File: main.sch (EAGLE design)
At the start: 18 parts, among them IC1 TINY45/85, U1 TMP102

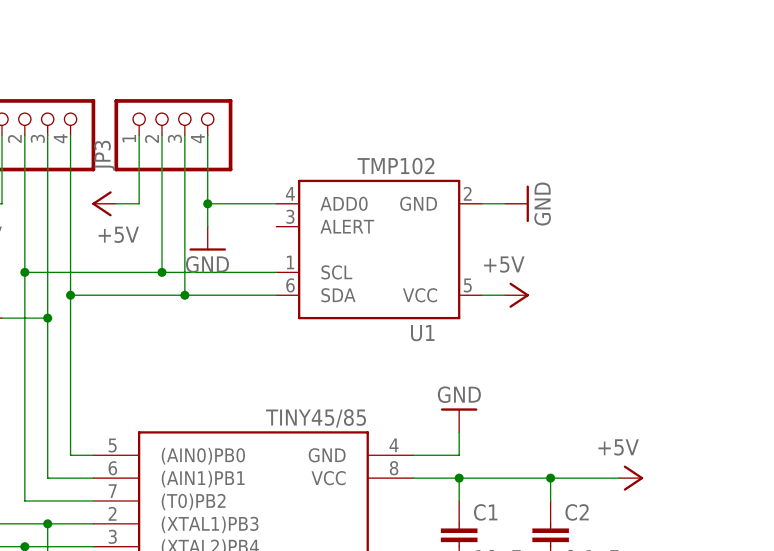
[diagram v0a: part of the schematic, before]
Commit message: changed sensor. sorted silk.
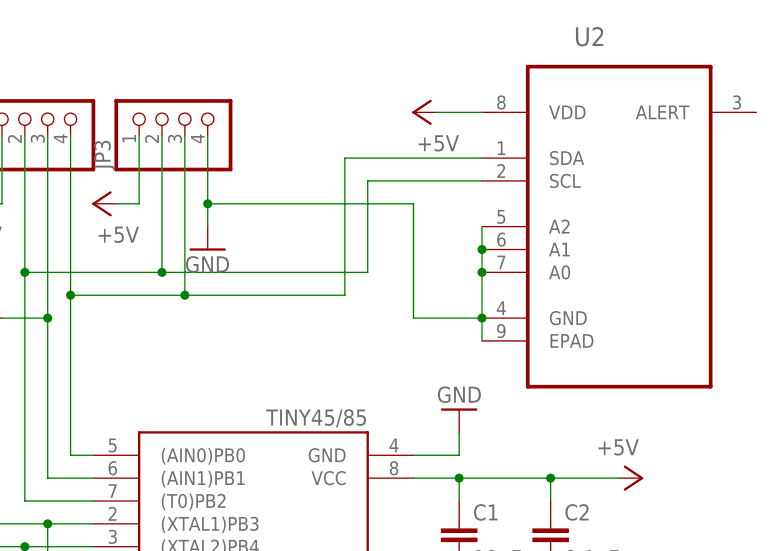
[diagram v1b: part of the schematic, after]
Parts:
- removed U1: TMP102, SparkFun-Sensors:TMP102
- added U2: MCP9808T-E/MC, mattsLib:MCP9808T-E/MC
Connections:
- net +5V: no longer U1.VCC
- net GND: now also U2.A0, U2.A1, U2.A2, U2.EPAD, U2.GND; no longer U1.ADD0, U1.GND
- net N$5: now also U2.SCL; no longer U1.SCL
- net N$9: now also U2.SDA; no longer U1.SDA
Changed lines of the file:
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@@
 <?xml version="1.0" encoding="utf-8"?>
 <!DOCTYPE eagle SYSTEM "eagle.dtd">
-<eagle version="7.2.0">
+<eagle version="7.0.0">
 <drawing>
 <settings>
@@
 <layer number="56" name="wert" color="7" fill="1" visible="no" active="no"/>
 <layer number="57" name="tCAD" color="7" fill="1" visible="no" active="no"/>
+<layer number="90" name="Modules" color="5" fill="1" visible="yes" active="yes"/>
 <layer number="91" name="Nets" color="2" fill="1" visible="yes" active="yes"/>
 <layer number="92" name="Busses" color="1" fill="1" visible="yes" active="yes"/>
@@
 <part name="GND8" library="supply1" deviceset="GND" device=""/>
 <part name="P+8" library="supply1" deviceset="+5V" device=""/>
-<part name="U1" library="SparkFun-Sensors" deviceset="TMP102" device="" value="TMP102"/>
-<part name="GND9" library="supply1" deviceset="GND" device=""/>
 <part name="CN1" library="adafruit" deviceset="USB" device="MINIB"/>
+<part name="U2" library="mattsLib" deviceset="MCP9808T-E/MC" device="" value=""/>
 </parts>
 <sheets>
@@
 <instance part="GND4" gate="1" x="-25.4" y="76.2" rot="R180"/>
 <instance part="GND5" gate="1" x="17.78" y="48.26" rot="R180"/>
-<instance part="P+5" gate="1" x="76.2" y="91.44" rot="R270"/>
+<instance part="P+5" gate="1" x="63.5" y="111.76" rot="R90"/>
 <instance part="P+6" gate="1" x="12.7" y="101.6" rot="R90"/>
 <instance part="GND6" gate="1" x="40.64" y="96.52"/>
@@
 <instance part="GND8" gate="1" x="7.62" y="104.14" rot="R180"/>
 <instance part="P+8" gate="1" x="27.94" y="101.6" rot="R90"/>
-<instance part="U1" gate="G$1" x="58.42" y="96.52" rot="R180"/>
-<instance part="GND9" gate="1" x="76.2" y="101.6" rot="R90"/>
 <instance part="CN1" gate="G$1" x="-38.1" y="66.04" rot="MR180"/>
+<instance part="U2" gate="A" x="86.36" y="101.6"/>
 </instances>
 <busses>
@@
 <pinref part="GND6" gate="1" pin="GND"/>
 <wire x1="40.64" y1="109.22" x2="40.64" y2="101.6" width="0.1524" layer="91"/>
-<pinref part="U1" gate="G$1" pin="ADD0"/>
 <wire x1="40.64" y1="101.6" x2="40.64" y2="99.06" width="0.1524" layer="91"/>
-<wire x1="48.26" y1="101.6" x2="40.64" y2="101.6" width="0.1524" layer="91"/>
 <junction x="40.64" y="101.6"/>
-</segment>
-<segment>
-<pinref part="U1" gate="G$1" pin="GND"/>
-<pinref part="GND9" gate="1" pin="GND"/>
-<wire x1="71.12" y1="101.6" x2="73.66" y2="101.6" width="0.1524" layer="91"/>
+<wire x1="40.64" y1="101.6" x2="63.5" y2="101.6" width="0.1524" layer="91"/>
+<wire x1="63.5" y1="101.6" x2="63.5" y2="88.9" width="0.1524" layer="91"/>
+<pinref part="U2" gate="A" pin="GND"/>
+<wire x1="63.5" y1="88.9" x2="71.12" y2="88.9" width="0.1524" layer="91"/>
+<pinref part="U2" gate="A" pin="EPAD"/>
+<wire x1="71.12" y1="88.9" x2="71.12" y2="86.36" width="0.1524" layer="91"/>
+<junction x="71.12" y="88.9"/>
+<pinref part="U2" gate="A" pin="A0"/>
+<wire x1="71.12" y1="88.9" x2="71.12" y2="93.98" width="0.1524" layer="91"/>
+<pinref part="U2" gate="A" pin="A1"/>
+<wire x1="71.12" y1="93.98" x2="71.12" y2="96.52" width="0.1524" layer="91"/>
+<pinref part="U2" gate="A" pin="A2"/>
+<wire x1="71.12" y1="96.52" x2="71.12" y2="99.06" width="0.1524" layer="91"/>
+<junction x="71.12" y="93.98"/>
+<junction x="71.12" y="96.52"/>
 </segment>
 </net>
@@
 <wire x1="25.4" y1="91.44" x2="25.4" y2="73.66" width="0.1524" layer="91"/>
 <wire x1="25.4" y1="73.66" x2="27.94" y2="73.66" width="0.1524" layer="91"/>
-<wire x1="48.26" y1="91.44" x2="38.1" y2="91.44" width="0.1524" layer="91"/>
+<wire x1="55.88" y1="91.44" x2="38.1" y2="91.44" width="0.1524" layer="91"/>
 <junction x="25.4" y="91.44"/>
 <pinref part="JP3" gate="A" pin="3"/>
@@
 <wire x1="38.1" y1="109.22" x2="38.1" y2="91.44" width="0.1524" layer="91"/>
 <junction x="38.1" y="91.44"/>
-<pinref part="U1" gate="G$1" pin="SDA"/>
+<wire x1="55.88" y1="91.44" x2="55.88" y2="106.68" width="0.1524" layer="91"/>
+<pinref part="U2" gate="A" pin="SDA"/>
+<wire x1="55.88" y1="106.68" x2="71.12" y2="106.68" width="0.1524" layer="91"/>
 </segment>
 </net>
@@
 </segment>
 <segment>
-<pinref part="U1" gate="G$1" pin="VCC"/>
 <pinref part="P+5" gate="1" pin="+5V"/>
-<wire x1="71.12" y1="91.44" x2="73.66" y2="91.44" width="0.1524" layer="91"/>
+<wire x1="71.12" y1="111.76" x2="66.04" y2="111.76" width="0.1524" layer="91"/>
 </segment>
 </net>
 <net name="N$5" class="0">
 <segment>
-<wire x1="48.26" y1="93.98" x2="35.56" y2="93.98" width="0.1524" layer="91"/>
+<wire x1="58.42" y1="93.98" x2="35.56" y2="93.98" width="0.1524" layer="91"/>
 <pinref part="JP3" gate="A" pin="2"/>
 <wire x1="35.56" y1="109.22" x2="35.56" y2="93.98" width="0.1524" layer="91"/>
@@
 <junction x="35.56" y="93.98"/>
 <junction x="20.32" y="93.98"/>
-<pinref part="U1" gate="G$1" pin="SCL"/>
-</segment>
-</net>
+<wire x1="58.42" y1="93.98" x2="58.42" y2="104.14" width="0.1524" layer="91"/>
+<pinref part="U2" gate="A" pin="SCL"/>
+<wire x1="58.42" y1="104.14" x2="71.12" y2="104.14" width="0.1524" layer="91"/>
+</segment>
+</net>

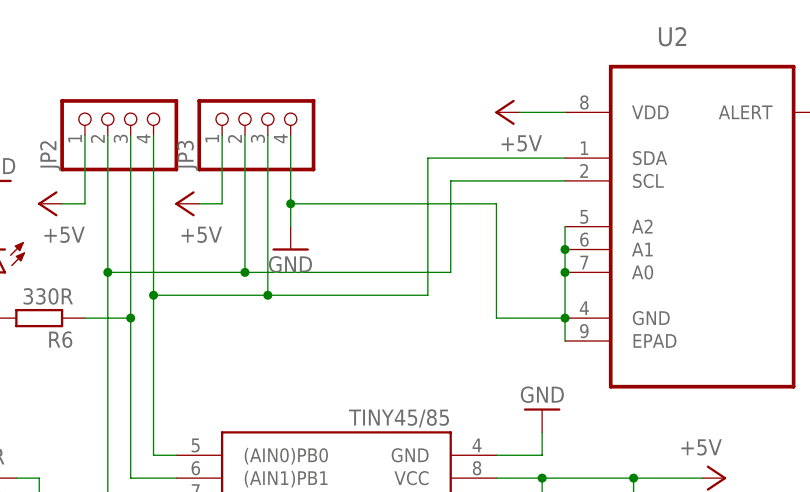
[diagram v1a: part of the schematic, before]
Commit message: Fixed text, added pull ups.
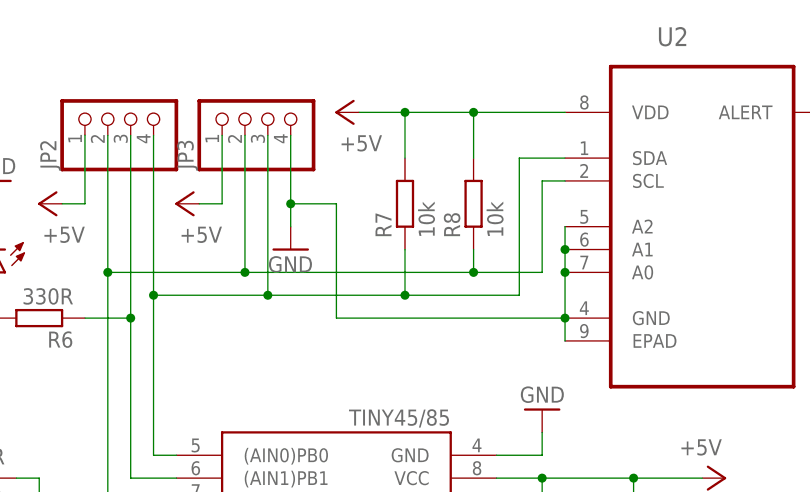
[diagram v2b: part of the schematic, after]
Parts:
- added R7, R8: 10k, resistor:R-EU_R0603
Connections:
- net +5V: now also R7.2, R8.2
- net N$5: now also R8.1
- net N$9: now also R7.1
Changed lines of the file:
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@@
 <part name="CN1" library="adafruit" deviceset="USB" device="MINIB"/>
 <part name="U2" library="mattsLib" deviceset="MCP9808T-E/MC" device="" value=""/>
+<part name="R7" library="resistor" deviceset="R-EU_" device="R0603" value="10k"/>
+<part name="R8" library="resistor" deviceset="R-EU_" device="R0603" value="10k"/>
 </parts>
 <sheets>
@@
 <instance part="GND4" gate="1" x="-25.4" y="76.2" rot="R180"/>
 <instance part="GND5" gate="1" x="17.78" y="48.26" rot="R180"/>
-<instance part="P+5" gate="1" x="63.5" y="111.76" rot="R90"/>
+<instance part="P+5" gate="1" x="45.72" y="111.76" rot="R90"/>
 <instance part="P+6" gate="1" x="12.7" y="101.6" rot="R90"/>
 <instance part="GND6" gate="1" x="40.64" y="96.52"/>
@@
 <instance part="CN1" gate="G$1" x="-38.1" y="66.04" rot="MR180"/>
 <instance part="U2" gate="A" x="86.36" y="101.6"/>
+<instance part="R7" gate="G$1" x="53.34" y="101.6" rot="R90"/>
+<instance part="R8" gate="G$1" x="60.96" y="101.6" rot="R90"/>
 </instances>
 <busses>
@@
 <wire x1="40.64" y1="101.6" x2="40.64" y2="99.06" width="0.1524" layer="91"/>
 <junction x="40.64" y="101.6"/>
-<wire x1="40.64" y1="101.6" x2="63.5" y2="101.6" width="0.1524" layer="91"/>
-<wire x1="63.5" y1="101.6" x2="63.5" y2="88.9" width="0.1524" layer="91"/>
+<wire x1="40.64" y1="101.6" x2="45.72" y2="101.6" width="0.1524" layer="91"/>
+<wire x1="45.72" y1="101.6" x2="45.72" y2="88.9" width="0.1524" layer="91"/>
 <pinref part="U2" gate="A" pin="GND"/>
-<wire x1="63.5" y1="88.9" x2="71.12" y2="88.9" width="0.1524" layer="91"/>
+<wire x1="45.72" y1="88.9" x2="71.12" y2="88.9" width="0.1524" layer="91"/>
 <pinref part="U2" gate="A" pin="EPAD"/>
 <wire x1="71.12" y1="88.9" x2="71.12" y2="86.36" width="0.1524" layer="91"/>
@@
 <wire x1="25.4" y1="91.44" x2="25.4" y2="73.66" width="0.1524" layer="91"/>
 <wire x1="25.4" y1="73.66" x2="27.94" y2="73.66" width="0.1524" layer="91"/>
-<wire x1="55.88" y1="91.44" x2="38.1" y2="91.44" width="0.1524" layer="91"/>
+<wire x1="66.04" y1="91.44" x2="53.34" y2="91.44" width="0.1524" layer="91"/>
 <junction x="25.4" y="91.44"/>
 <pinref part="JP3" gate="A" pin="3"/>
+<wire x1="53.34" y1="91.44" x2="38.1" y2="91.44" width="0.1524" layer="91"/>
 <wire x1="38.1" y1="91.44" x2="25.4" y2="91.44" width="0.1524" layer="91"/>
 <wire x1="38.1" y1="109.22" x2="38.1" y2="91.44" width="0.1524" layer="91"/>
 <junction x="38.1" y="91.44"/>
-<wire x1="55.88" y1="91.44" x2="55.88" y2="106.68" width="0.1524" layer="91"/>
+<wire x1="66.04" y1="91.44" x2="66.04" y2="106.68" width="0.1524" layer="91"/>
 <pinref part="U2" gate="A" pin="SDA"/>
-<wire x1="55.88" y1="106.68" x2="71.12" y2="106.68" width="0.1524" layer="91"/>
+<wire x1="66.04" y1="106.68" x2="71.12" y2="106.68" width="0.1524" layer="91"/>
+<pinref part="R7" gate="G$1" pin="1"/>
+<wire x1="53.34" y1="96.52" x2="53.34" y2="91.44" width="0.1524" layer="91"/>
+<junction x="53.34" y="91.44"/>
 </segment>
 </net>
@@
 <segment>
 <pinref part="P+5" gate="1" pin="+5V"/>
-<wire x1="71.12" y1="111.76" x2="66.04" y2="111.76" width="0.1524" layer="91"/>
+<wire x1="71.12" y1="111.76" x2="60.96" y2="111.76" width="0.1524" layer="91"/>
+<pinref part="R7" gate="G$1" pin="2"/>
+<wire x1="60.96" y1="111.76" x2="53.34" y2="111.76" width="0.1524" layer="91"/>
+<wire x1="53.34" y1="111.76" x2="48.26" y2="111.76" width="0.1524" layer="91"/>
+<wire x1="53.34" y1="111.76" x2="53.34" y2="106.68" width="0.1524" layer="91"/>
+<pinref part="R8" gate="G$1" pin="2"/>
+<wire x1="60.96" y1="111.76" x2="60.96" y2="106.68" width="0.1524" layer="91"/>
+<junction x="53.34" y="111.76"/>
+<junction x="60.96" y="111.76"/>
 </segment>
 </net>
 <net name="N$5" class="0">
 <segment>
-<wire x1="58.42" y1="93.98" x2="35.56" y2="93.98" width="0.1524" layer="91"/>
+<wire x1="68.58" y1="93.98" x2="60.96" y2="93.98" width="0.1524" layer="91"/>
 <pinref part="JP3" gate="A" pin="2"/>
+<wire x1="60.96" y1="93.98" x2="35.56" y2="93.98" width="0.1524" layer="91"/>
 <wire x1="35.56" y1="109.22" x2="35.56" y2="93.98" width="0.1524" layer="91"/>
 <pinref part="IC1" gate="G$1" pin="(T0)PB2"/>
@@
 <junction x="35.56" y="93.98"/>
 <junction x="20.32" y="93.98"/>
-<wire x1="58.42" y1="93.98" x2="58.42" y2="104.14" width="0.1524" layer="91"/>
+<wire x1="68.58" y1="93.98" x2="68.58" y2="104.14" width="0.1524" layer="91"/>
 <pinref part="U2" gate="A" pin="SCL"/>
-<wire x1="58.42" y1="104.14" x2="71.12" y2="104.14" width="0.1524" layer="91"/>
-</segment>
-</net>
+<wire x1="68.58" y1="104.14" x2="71.12" y2="104.14" width="0.1524" layer="91"/>
+<pinref part="R8" gate="G$1" pin="1"/>
+<wire x1="60.96" y1="96.52" x2="60.96" y2="93.98" width="0.1524" layer="91"/>
+<junction x="60.96" y="93.98"/>
+</segment>
+</net>

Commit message: Pulled BoM.xlsx, also changed pull ups to 0805
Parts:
- R7, R8: device resistor:R-EU_R0603 -> resistor:R-EU_R0805
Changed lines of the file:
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@@
 <grid distance="0.1" unitdist="inch" unit="inch" style="lines" multiple="1" display="no" altdistance="0.01" altunitdist="inch" altunit="inch"/>
 <layers>
-<layer number="1" name="Top" color="4" fill="1" visible="no" active="no"/>
-<layer number="2" name="Route2" color="1" fill="3" visible="no" active="no"/>
-<layer number="3" name="Route3" color="4" fill="3" visible="no" active="no"/>
-<layer number="4" name="Route4" color="1" fill="4" visible="no" active="no"/>
-<layer number="5" name="Route5" color="4" fill="4" visible="no" active="no"/>
-<layer number="6" name="Route6" color="1" fill="8" visible="no" active="no"/>
-<layer number="7" name="Route7" color="4" fill="8" visible="no" active="no"/>
-<layer number="8" name="Route8" color="1" fill="2" visible="no" active="no"/>
-<layer number="9" name="Route9" color="4" fill="2" visible="no" active="no"/>
-<layer number="10" name="Route10" color="1" fill="7" visible="no" active="no"/>
-<layer number="11" name="Route11" color="4" fill="7" visible="no" active="no"/>
-<layer number="12" name="Route12" color="1" fill="5" visible="no" active="no"/>
-<layer number="13" name="Route13" color="4" fill="5" visible="no" active="no"/>
-<layer number="14" name="Route14" color="1" fill="6" visible="no" active="no"/>
-<layer number="15" name="Route15" color="4" fill="6" visible="no" active="no"/>
-<layer number="16" name="Bottom" color="1" fill="1" visible="no" active="no"/>
-<layer number="17" name="Pads" color="2" fill="1" visible="no" active="no"/>
-<layer number="18" name="Vias" color="2" fill="1" visible="no" active="no"/>
-<layer number="19" name="Unrouted" color="6" fill="1" visible="no" active="no"/>
-<layer number="20" name="Dimension" color="15" fill="1" visible="no" active="no"/>
-<layer number="21" name="tPlace" color="7" fill="1" visible="no" active="no"/>
-<layer number="22" name="bPlace" color="7" fill="1" visible="no" active="no"/>
-<layer number="23" name="tOrigins" color="15" fill="1" visible="no" active="no"/>
-<layer number="24" name="bOrigins" color="15" fill="1" visible="no" active="no"/>
-<layer number="25" name="tNames" color="7" fill="1" visible="no" active="no"/>
-<layer number="26" name="bNames" color="7" fill="1" visible="no" active="no"/>
-<layer number="27" name="tValues" color="7" fill="1" visible="no" active="no"/>
-<layer number="28" name="bValues" color="7" fill="1" visible="no" active="no"/>
+<layer number="1" name="Top" color="4" fill="1" visible="yes" active="no"/>
+<layer number="2" name="Route2" color="1" fill="3" visible="yes" active="no"/>
+<layer number="3" name="Route3" color="4" fill="3" visible="yes" active="no"/>
+<layer number="4" name="Route4" color="1" fill="4" visible="yes" active="no"/>
+<layer number="5" name="Route5" color="4" fill="4" visible="yes" active="no"/>
+<layer number="6" name="Route6" color="1" fill="8" visible="yes" active="no"/>
+<layer number="7" name="Route7" color="4" fill="8" visible="yes" active="no"/>
+<layer number="8" name="Route8" color="1" fill="2" visible="yes" active="no"/>
+<layer number="9" name="Route9" color="4" fill="2" visible="yes" active="no"/>
+<layer number="10" name="Route10" color="1" fill="7" visible="yes" active="no"/>
+<layer number="11" name="Route11" color="4" fill="7" visible="yes" active="no"/>
+<layer number="12" name="Route12" color="1" fill="5" visible="yes" active="no"/>
+<layer number="13" name="Route13" color="4" fill="5" visible="yes" active="no"/>
+<layer number="14" name="Route14" color="1" fill="6" visible="yes" active="no"/>
+<layer number="15" name="Route15" color="4" fill="6" visible="yes" active="no"/>
+<layer number="16" name="Bottom" color="1" fill="1" visible="yes" active="no"/>
+<layer number="17" name="Pads" color="2" fill="1" visible="yes" active="no"/>
+<layer number="18" name="Vias" color="2" fill="1" visible="yes" active="no"/>
+<layer number="19" name="Unrouted" color="6" fill="1" visible="yes" active="no"/>
+<layer number="20" name="Dimension" color="15" fill="1" visible="yes" active="no"/>
+<layer number="21" name="tPlace" color="7" fill="1" visible="yes" active="no"/>
+<layer number="22" name="bPlace" color="7" fill="1" visible="yes" active="no"/>
+<layer number="23" name="tOrigins" color="15" fill="1" visible="yes" active="no"/>
+<layer number="24" name="bOrigins" color="15" fill="1" visible="yes" active="no"/>
+<layer number="25" name="tNames" color="7" fill="1" visible="yes" active="no"/>
+<layer number="26" name="bNames" color="7" fill="1" visible="yes" active="no"/>
+<layer number="27" name="tValues" color="7" fill="1" visible="yes" active="no"/>
+<layer number="28" name="bValues" color="7" fill="1" visible="yes" active="no"/>
 <layer number="29" name="tStop" color="7" fill="3" visible="no" active="no"/>
 <layer number="30" name="bStop" color="7" fill="6" visible="no" active="no"/>
@@
 <layer number="35" name="tGlue" color="7" fill="4" visible="no" active="no"/>
 <layer number="36" name="bGlue" color="7" fill="5" visible="no" active="no"/>
-<layer number="37" name="tTest" color="7" fill="1" visible="no" active="no"/>
-<layer number="38" name="bTest" color="7" fill="1" visible="no" active="no"/>
+<layer number="37" name="tTest" color="7" fill="1" visible="yes" active="no"/>
+<layer number="38" name="bTest" color="7" fill="1" visible="yes" active="no"/>
 <layer number="39" name="tKeepout" color="4" fill="11" visible="no" active="no"/>
 <layer number="40" name="bKeepout" color="1" fill="11" visible="no" active="no"/>
@@
 <layer number="44" name="Drills" color="7" fill="1" visible="no" active="no"/>
 <layer number="45" name="Holes" color="7" fill="1" visible="no" active="no"/>
-<layer number="46" name="Milling" color="3" fill="1" visible="no" active="no"/>
-<layer number="47" name="Measures" color="7" fill="1" visible="no" active="no"/>
-<layer number="48" name="Document" color="7" fill="1" visible="no" active="no"/>
-<layer number="49" name="Reference" color="7" fill="1" visible="no" active="no"/>
-<layer number="50" name="dxf" color="7" fill="1" visible="no" active="no"/>
-<layer number="51" name="tDocu" color="7" fill="1" visible="no" active="no"/>
-<layer number="52" name="bDocu" color="7" fill="1" visible="no" active="no"/>
-<layer number="53" name="tGND_GNDA" color="7" fill="9" visible="no" active="no"/>
-<layer number="54" name="bGND_GNDA" color="1" fill="9" visible="no" active="no"/>
-<layer number="56" name="wert" color="7" fill="1" visible="no" active="no"/>
-<layer number="57" name="tCAD" color="7" fill="1" visible="no" active="no"/>
+<layer number="46" name="Milling" color="3" fill="1" visible="yes" active="no"/>
+<layer number="47" name="Measures" color="7" fill="1" visible="yes" active="no"/>
+<layer number="48" name="Document" color="7" fill="1" visible="yes" active="no"/>
+<layer number="49" name="Reference" color="7" fill="1" visible="yes" active="no"/>
+<layer number="50" name="dxf" color="7" fill="1" visible="yes" active="no"/>
+<layer number="51" name="tDocu" color="7" fill="1" visible="yes" active="no"/>
+<layer number="52" name="bDocu" color="7" fill="1" visible="yes" active="no"/>
+<layer number="53" name="tGND_GNDA" color="7" fill="9" visible="yes" active="no"/>
+<layer number="54" name="bGND_GNDA" color="1" fill="9" visible="yes" active="no"/>
+<layer number="56" name="wert" color="7" fill="1" visible="yes" active="no"/>
+<layer number="57" name="tCAD" color="7" fill="1" visible="yes" active="no"/>
 <layer number="90" name="Modules" color="5" fill="1" visible="yes" active="yes"/>
 <layer number="91" name="Nets" color="2" fill="1" visible="yes" active="yes"/>
@@
 <part name="CN1" library="adafruit" deviceset="USB" device="MINIB"/>
 <part name="U2" library="mattsLib" deviceset="MCP9808T-E/MC" device="" value=""/>
-<part name="R7" library="resistor" deviceset="R-EU_" device="R0603" value="10k"/>
-<part name="R8" library="resistor" deviceset="R-EU_" device="R0603" value="10k"/>
+<part name="R7" library="resistor" deviceset="R-EU_" device="R0805" value="10k"/>
+<part name="R8" library="resistor" deviceset="R-EU_" device="R0805" value="10k"/>
 </parts>
 <sheets>
